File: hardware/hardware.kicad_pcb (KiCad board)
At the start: 2 copper layers, 91.4 x 91.4 mm, 80 parts, among them J1 DB25_Female, J2 USB_B_Micro, J3 RJ45_Bel_SI-60062-F-68net, J4 Conn_02x06_Odd_Even, U1 LD1117S33TR_SOT223, U11 ENC28J60x-SO, U12 74HC14, U2 74LS126, U3 74LS126, U4 LM1117-ADJ, U5 74LS126, U6 74LS126, U7 STM32F072R8Tx, U8 74LS245, Y1 8MHz, Y2 25MHz

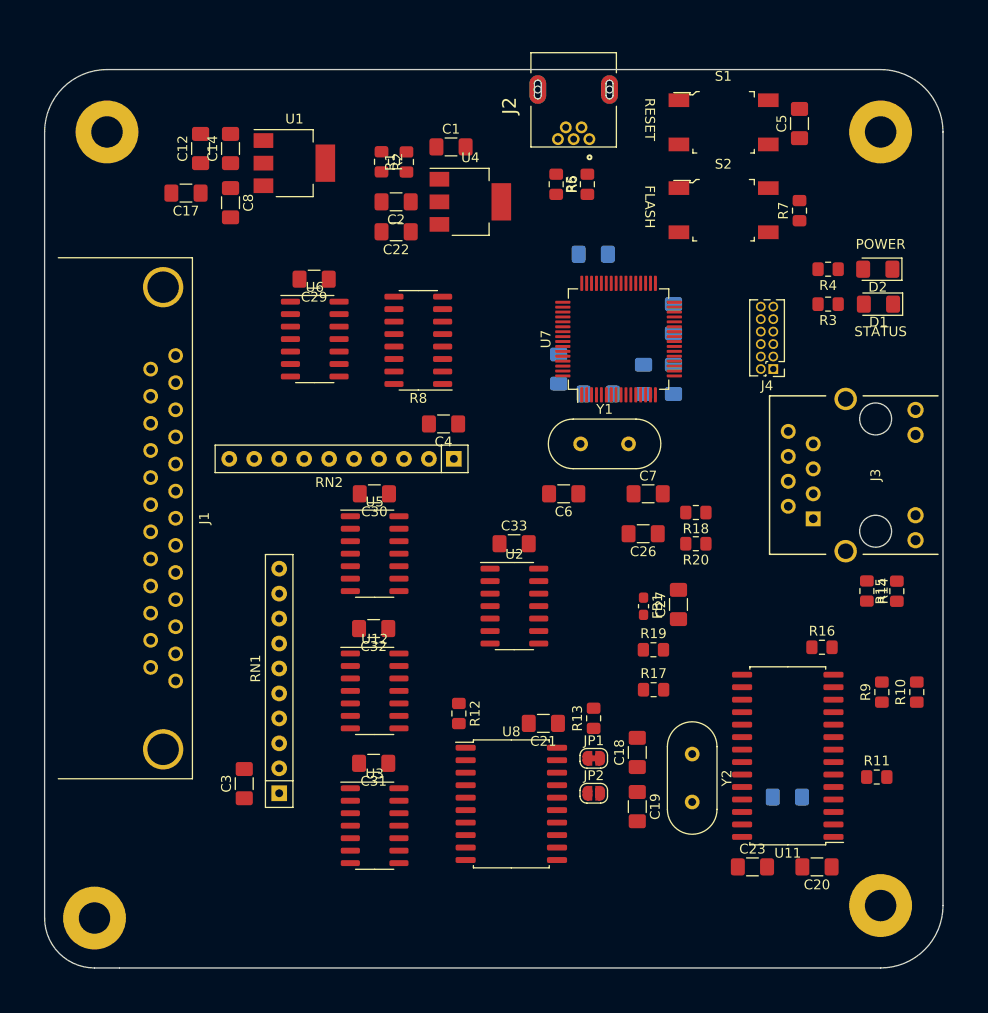
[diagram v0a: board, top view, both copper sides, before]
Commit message: feat: update extension port and place again footprints on pcb
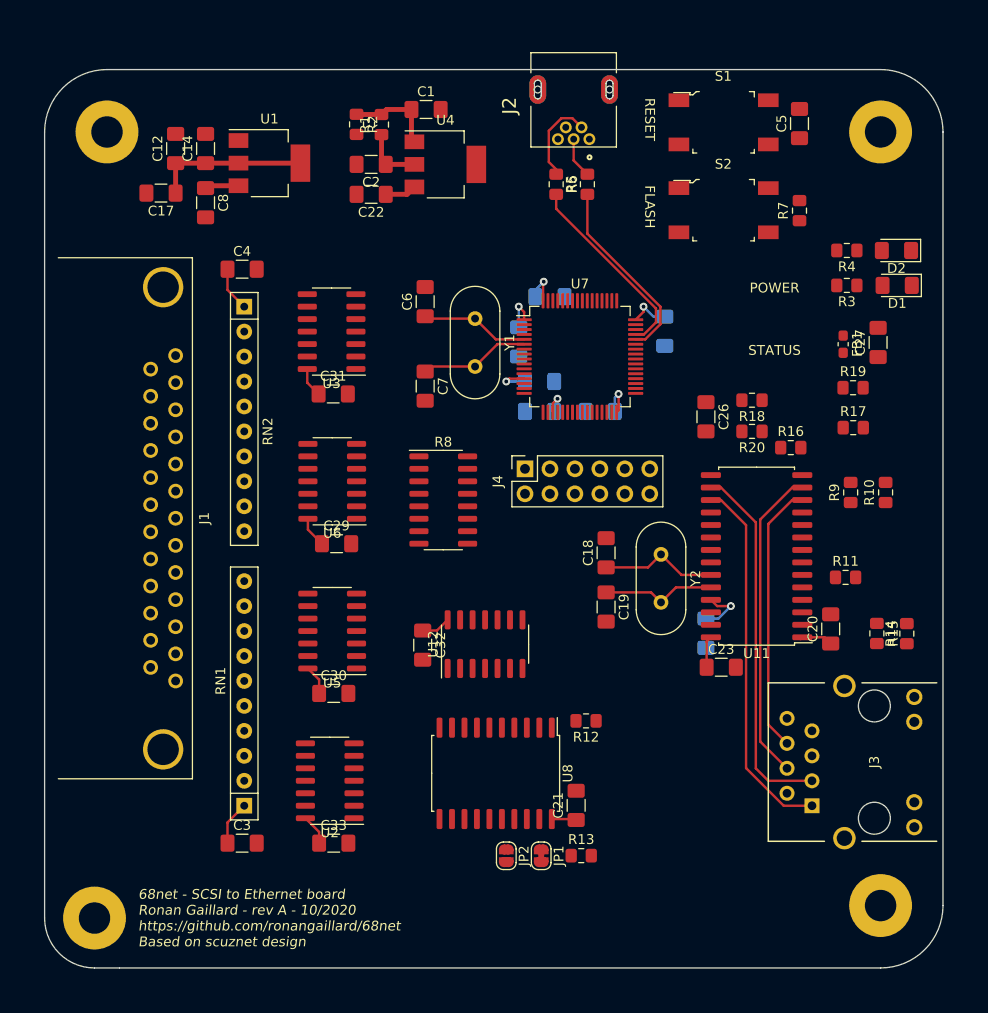
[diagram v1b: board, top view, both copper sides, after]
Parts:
- J4: footprint Connector_PinHeader_1.27mm:PinHeader_2x06_P1.27mm_Vertical -> Connector_PinSocket_2.54mm:PinSocket_2x06_P2.54mm_Vertical
- moved U3 50.5 mm to (49.5, 47.0), turned to 180 degrees
- moved C31 37.8 mm to (49.7, 53.3), turned to 0 degrees
- moved C33 35.6 mm to (49.7, 99.1)
- moved C27 33.5 mm to (105.2, 48.1)
- moved FB1 33.5 mm to (101.6, 48.3)
- moved R19 33.5 mm to (102.6, 52.7)
- moved R17 33.5 mm to (102.6, 56.8)
- moved J3 29.2 mm to (104.8, 96.5)
- moved J4 27.2 mm to (69.2, 61.0), turned to 90 degrees
- moved C29 27.0 mm to (50.0, 68.6), turned to 0 degrees
- moved RN2 26.4 mm to (40.6, 44.5), turned to 270 degrees
- moved U2 25.9 mm to (49.3, 92.7), turned to 180 degrees
- moved C4 25.9 mm to (40.4, 40.6), turned to 0 degrees
- moved C7 25.2 mm to (59.1, 52.5), turned to 270 degrees
- moved C20 24.3 mm to (100.3, 77.3), turned to 90 degrees
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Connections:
- net /DCLK renamed Net-(U7-Pad62)
- net /~DOE~ renamed Net-(U7-Pad29)
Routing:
- net +3V3: track 0.00 -> 64.6 mm, vias 0 -> 7
- net /TPOUT+: track 0.00 -> 37.7 mm
- net /TPOUT-: track 0.00 -> 37.3 mm
- net /TPIN+: track 0.00 -> 32.1 mm
- net /TPIN-: track 0.00 -> 27.6 mm
- net /USB+: track 0.00 -> 19.8 mm
- net /USB-: track 0.00 -> 19.5 mm
- net VBUS: track 0.00 -> 15.2 mm
- net Net-(C18-Pad1): track 0.00 -> 12.1 mm
- net Net-(C19-Pad1): track 0.00 -> 11.7 mm
- net Net-(C7-Pad1): track 0.00 -> 11.2 mm
- net Net-(C6-Pad1): track 0.00 -> 11.0 mm
- net Net-(C1-Pad1): track 0.00 -> 9.22 mm
- net Net-(J2-Pad2): track 0.00 -> 8.97 mm
- net +5V: track 0.00 -> 6.68 mm
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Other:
- board text added: "68net - SCSI to Ethernet board Ronan Gaillard - rev A - 10/2020 https://github.com/ronangaillard/68net Based on scuznet design"

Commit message: feat: finalize revA-alpha
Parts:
- removed J4: Conn_02x06_Odd_Even, Connector_PinSocket_2.54mm:PinSocket_2x06_P2.54mm_Vertical
- removed JP1: SJ, Jumper:SolderJumper-2_P1.3mm_Bridged_RoundedPad1.0x1.5mm
- removed JP2: SJ, Jumper:SolderJumper-2_P1.3mm_Open_RoundedPad1.0x1.5mm
- removed R11: 22, Resistor_SMD:R_0805_2012Metric_Pad1.15x1.40mm_HandSolder
- removed REF00, REF01, REF02, REF03: MountingHole_3.2mm_M3_Pad, MountingHole:MountingHole_3.2mm_M3_Pad
- added C25: 100uF, Capacitor_SMD:CP_Elec_6.3x5.4, F.Cu at (34.3, 28.4)
- added C28: 100nF, Capacitor_SMD:C_1206_3216Metric_Pad1.42x1.75mm_HandSolder, F.Cu at (67.3, 97.5)
- added C34: 100nF, Capacitor_SMD:C_1206_3216Metric_Pad1.42x1.75mm_HandSolder, B.Cu at (79.2, 98.8)
- added C35: 100nF, Capacitor_SMD:C_1206_3216Metric_Pad1.42x1.75mm_HandSolder, B.Cu at (72.9, 98.8)
- added D3: D_Schottky, Diode_SMD:D_SOD-523, F.Cu at (71.7, 35.6)
- added D4: D_Schottky, Diode_SMD:D_SOD-523, F.Cu at (39.9, 35.6)
- added G***: LOGO, hardware:Untitled, F.Cu at (84.8, 45.5)
- added H1: MountingHole, MountingHole:MountingHole_3.2mm_M3_Pad, F.Cu at (105.4, 26.7)
- added H2: MountingHole, MountingHole:MountingHole_3.2mm_M3_Pad, F.Cu at (105.4, 105.4)
- added H3: MountingHole, MountingHole:MountingHole_3.2mm_M3_Pad, F.Cu at (26.7, 26.7)
- added H4: MountingHole, MountingHole:MountingHole_3.2mm_M3_Pad, F.Cu at (26.7, 105.4)
- added R21: 3k3, Resistor_SMD:R_0805_2012Metric_Pad1.15x1.40mm_HandSolder, F.Cu at (46.0, 62.2)
- added R22: 3k3, Resistor_SMD:R_0805_2012Metric_Pad1.15x1.40mm_HandSolder, F.Cu at (46.0, 53.3)
- added R23: 3k3, Resistor_SMD:R_0805_2012Metric_Pad1.15x1.40mm_HandSolder, F.Cu at (46.0, 55.9)
- added R24: 3k3, Resistor_SMD:R_0805_2012Metric_Pad1.15x1.40mm_HandSolder, F.Cu at (46.0, 48.9)
- added R25: 3k3, Resistor_SMD:R_0805_2012Metric_Pad1.15x1.40mm_HandSolder, F.Cu at (46.0, 46.4)
- added R26: 3k3, Resistor_SMD:R_0805_2012Metric_Pad1.15x1.40mm_HandSolder, F.Cu at (46.0, 43.2)
- added R27: 3k3, Resistor_SMD:R_0805_2012Metric_Pad1.15x1.40mm_HandSolder, F.Cu at (46.0, 40.6)
- added R28: 3k3, Resistor_SMD:R_0805_2012Metric_Pad1.15x1.40mm_HandSolder, F.Cu at (68.1, 59.7)
- added R29: 3k3, Resistor_SMD:R_0805_2012Metric_Pad1.15x1.40mm_HandSolder, F.Cu at (58.2, 68.6)
- added R30: 3k3, Resistor_SMD:R_0805_2012Metric_Pad1.15x1.40mm_HandSolder, F.Cu at (58.2, 73.7)
- added R31: 3k3, Resistor_SMD:R_0805_2012Metric_Pad1.15x1.40mm_HandSolder, F.Cu at (46.0, 85.1)
- added R32: 3k3, Resistor_SMD:R_0805_2012Metric_Pad1.15x1.40mm_HandSolder, F.Cu at (46.0, 87.6)
- added R33: 3k3, Resistor_SMD:R_0805_2012Metric_Pad1.15x1.40mm_HandSolder, F.Cu at (46.0, 94.0)
- added R34: 3k3, Resistor_SMD:R_0805_2012Metric_Pad1.15x1.40mm_HandSolder, F.Cu at (46.0, 96.5)
- R4: value 330 -> 165
- R8: value resistor_array_15 -> 3k3; footprint Package_SO:SOIC-16_3.9x9.9mm_P1.27mm -> Resistor_SMD:R_0805_2012Metric_Pad1.15x1.40mm_HandSolder
- U1: value LD1117S33TR_SOT223 -> LD1117 3.3
- U12: value 74HC14 -> 74LVC14
- U2, U3, U5, U6: value 74LS126 -> 74LVTH126
- U8: value 74LS245 -> 74LVC245
- moved FB1 68.9 mm to (62.4, 104.9), turned to 0 degrees
- moved C27 68.8 mm to (62.2, 101.9), turned to 180 degrees
- moved J2 62.6 mm to (110.0, 73.7), turned to 0 degrees
- moved R19 62.1 mm to (67.1, 103.6), turned to 90 degrees
- moved R17 57.2 mm to (69.8, 103.6), turned to 90 degrees
- moved C6 54.2 mm to (108.8, 65.3), turned to 270 degrees
- moved C7 50.0 mm to (108.8, 56.7), turned to 90 degrees
- moved R13 48.4 mm to (63.2, 53.3), turned to 270 degrees
- moved U3 47.1 mm to (53.3, 94.0), turned to 0 degrees
- moved U8 46.4 mm to (71.9, 45.9), turned to 180 degrees
- moved R6 45.6 mm to (97.8, 69.9), turned to 90 degrees
- moved R5 45.4 mm to (100.6, 69.8), turned to 270 degrees
- moved Y1 43.5 mm to (103.8, 63.6), turned to 90 degrees
- moved R16 42.8 mm to (67.6, 90.6), turned to 90 degrees
- moved C21 41.5 mm to (68.6, 54.1), turned to 0 degrees
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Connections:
- C22 pad 1: +5V -> VCC
- C8 pad 1: +5V -> VCC
- J1 pad 25: Net-(J1-Pad25) -> /TPWR
- R13 pad 1: Net-(JP1-Pad2) -> Net-(R13-Pad1)
- R4 pad 2: +5V -> +3V3
- R8 pad 1: /TDB0 -> GND
- R8 pad 2: /TDB1 -> /TDB0
- U1 pad 3: +5V -> VCC
- U11 pad 6: Net-(R11-Pad1) -> /SPI_MISO
- U2 pad 1: /TBSY -> /TDBP
- U2 pad 10: /TDB0 -> GND
- U2 pad 11: /DB4 -> /SEL
- U2 pad 13: /TDB4 -> /TSEL
- U2 pad 3: /BSY -> /DBP
- U2 pad 4: /TREQ -> /TBSY
- U2 pad 6: /REQ -> /BSY
- U2 pad 8: /DB0 -> Net-(U2-Pad8)
- U3 pad 1: GND -> /TIO
- U3 pad 10: /TDB1 -> /TREQ
- U3 pad 11: /DB5 -> /CD
- U3 pad 13: /TDB5 -> /TCD
- U3 pad 3: Net-(U3-Pad3) -> /IO
- U3 pad 8: /DB1 -> /REQ
- U4 pad 3: +5V -> VCC
- U5 pad 1: /TSEL -> /TDB3
- U5 pad 10: /TDB2 -> /TDB0
- U5 pad 11: /DB6 -> /DB2
- U5 pad 13: /TDB6 -> /TDB2
- U5 pad 3: /SEL -> /DB3
- U5 pad 4: /TCD -> /TDB1
- U5 pad 6: /CD -> /DB1
- U5 pad 8: /DB2 -> /DB0
- U6 pad 1: /TDBP -> /TDB7
- U6 pad 10: /TDB3 -> /TDB4
- U6 pad 11: /DB7 -> /DB6
- U6 pad 13: /TDB7 -> /TDB6
- U6 pad 3: /DBP -> /DB7
- U6 pad 4: /TIO -> /TDB5
- U6 pad 6: /IO -> /DB5
- U6 pad 8: /DB3 -> /DB4
- U7 pad 10: /RDB2 -> Net-(U7-Pad10)
- U7 pad 11: /RDB3 -> Net-(U7-Pad11)
- U7 pad 14: /TDB0 -> /RDB0
- U7 pad 15: /TDB1 -> /RDB1
- U7 pad 16: /TDB2 -> /RDB2
- U7 pad 17: /TDB3 -> /RDB3
- U7 pad 2: Net-(U7-Pad2) -> /STATUS_LED
- U7 pad 20: /TDB4 -> /RDB4
- U7 pad 21: /TDB5 -> /RDB5
- U7 pad 22: /TDB6 -> /RDB6
- U7 pad 23: /TDB7 -> /RDB7
- U7 pad 24: /RDB4 -> Net-(U7-Pad24)
- U7 pad 25: /RDB5 -> Net-(U7-Pad25)
- U7 pad 26: /TREQ -> /TDB0
- U7 pad 27: /RDBP -> /TDB1
- U7 pad 28: /RSEL -> /TDB2
- U7 pad 3: /RACK -> Net-(U7-Pad3)
- U7 pad 30: /~SPI_INT~ -> Net-(U7-Pad30)
- U7 pad 37: /RDB6 -> /TDBP
- U7 pad 38: /RDB7 -> /TSEL
- U7 pad 39: /RDBP -> /TBSY
- U7 pad 4: /STATUS_LED -> Net-(U7-Pad4)
- U7 pad 40: /GPIO_0 -> /RDBP
- U7 pad 41: /TDBP -> /RSEL
- U7 pad 42: /TSEL -> /RBSY
- U7 pad 43: /TBSY -> /RACK
- U7 pad 46: /TCD -> /RATN
- U7 pad 49: /TIO -> /RRST
- U7 pad 50: /TMSG -> /TIO
- U7 pad 51: /GPIO_1 -> /TCD
- U7 pad 52: /GPIO_2 -> /TMSG
- U7 pad 53: /GPIO_3 -> /TREQ
- U7 pad 55: /RBSY -> /TDB3
- U7 pad 56: /RATN -> /TDB4
- U7 pad 57: /RRST -> /TDB5
- U7 pad 58: /UART_TX -> /TDB6
- U7 pad 59: /UART_RX -> /TDB7
- U7 pad 62: Net-(U7-Pad62) -> /~SPI_INT~
- U7 pad 8: /RDB0 -> Net-(U7-Pad8)
- U7 pad 9: /RDB1 -> Net-(U7-Pad9)
- U8 pad 11: /DB0 -> /DB7
- U8 pad 12: /DB1 -> /DB6
- U8 pad 13: /DB2 -> /DB5
- U8 pad 14: /DB3 -> /DB4
- U8 pad 15: /DB4 -> /DB3
- U8 pad 16: /DB5 -> /DB2
- U8 pad 17: /DB6 -> /DB1
- U8 pad 18: /DB7 -> /DB0
- U8 pad 19: Net-(JP1-Pad1) -> Net-(R13-Pad1)
- U8 pad 2: /RDB7 -> /RDB0
- U8 pad 3: /RDB6 -> /RDB1
- U8 pad 4: /RDB5 -> /RDB2
- U8 pad 5: /RDB4 -> /RDB3
- U8 pad 6: /RDB3 -> /RDB4
- U8 pad 7: /RDB2 -> /RDB5
- U8 pad 8: /RDB1 -> /RDB6
- U8 pad 9: /RDB0 -> /RDB7
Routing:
- net +3V3: track 64.6 -> 504.1 mm, vias 7 -> 19
- net GND: track 0.00 -> 104.5 mm, vias 0 -> 393
- net /BOOT0: track 0.00 -> 87.6 mm
- net VBUS: track 15.2 -> 102.4 mm, vias 0 -> 2
- net /TDB6: track 0.00 -> 81.3 mm, vias 0 -> 2
- net /TDB7: track 0.00 -> 80.7 mm, vias 0 -> 2
- net /TDB5: track 0.00 -> 77.6 mm, vias 0 -> 2
- net /TDB4: track 0.00 -> 73.4 mm, vias 0 -> 2
- net /TCD: track 0.00 -> 66.8 mm, vias 0 -> 2
- net /TREQ: track 0.00 -> 63.8 mm, vias 0 -> 2
- net +5V: track 6.68 -> 69.2 mm, vias 0 -> 4
- net /TMSG: track 0.00 -> 62.5 mm, vias 0 -> 2
- net /TIO: track 0.00 -> 59.9 mm, vias 0 -> 2
- net /TDB3: track 0.00 -> 59.8 mm, vias 0 -> 2
- net /TDB2: track 0.00 -> 57.7 mm, vias 0 -> 2
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- added copper zone on B.Cu, net GND
- added copper zone on F.Cu, net GND
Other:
- outline, holes or cut-outs redrawn
- board text added: "68net"
- board text added: "Modern SCSI2Ethernet"

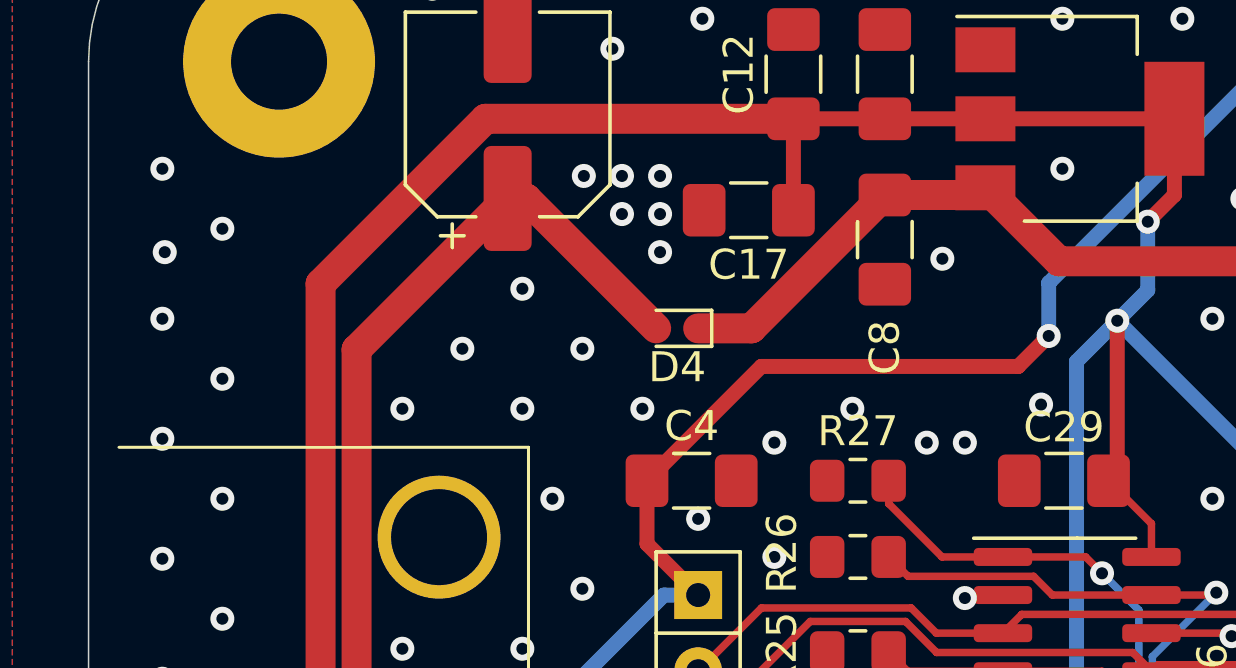
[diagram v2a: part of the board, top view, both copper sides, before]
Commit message: feat: add jumper connector to enable termination
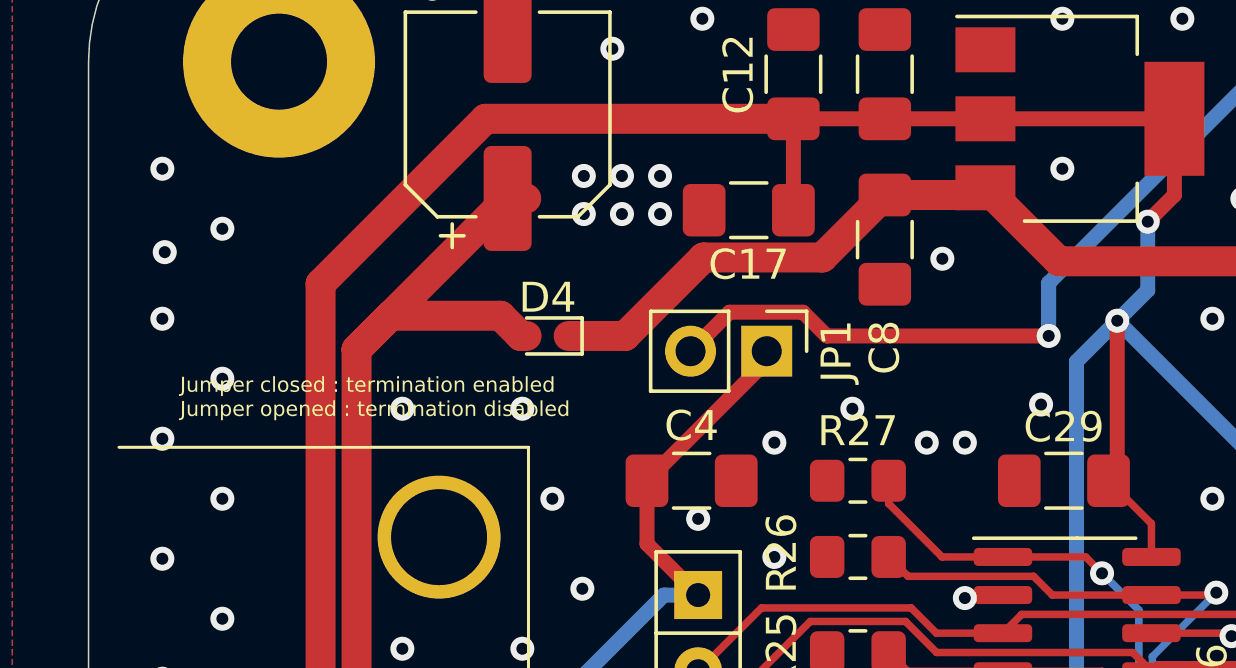
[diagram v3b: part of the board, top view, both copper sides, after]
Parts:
- added JP1: Jumper_2_Bridged, Connector_PinHeader_2.54mm:PinHeader_1x02_P2.54mm_Vertical, F.Cu at (42.9, 36.3)
- moved D4 4.33 mm to (35.6, 35.8)
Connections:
- C3 pad 1: VBUS -> Net-(C3-Pad1)
- C4 pad 1: VBUS -> Net-(C3-Pad1)
- RN1 pad 1: VBUS -> Net-(C3-Pad1)
- RN2 pad 1: VBUS -> Net-(C3-Pad1)
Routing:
- net Net-(C3-Pad1): track 0.00 -> 69.7 mm
- net VBUS: track 102.4 -> 36.1 mm
- net VCC: track 38.0 -> 42.4 mm
- net GND: vias 393 -> 389
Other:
- board text added: "Jumper closed : termination enabled Jumper opened : termination disabled"

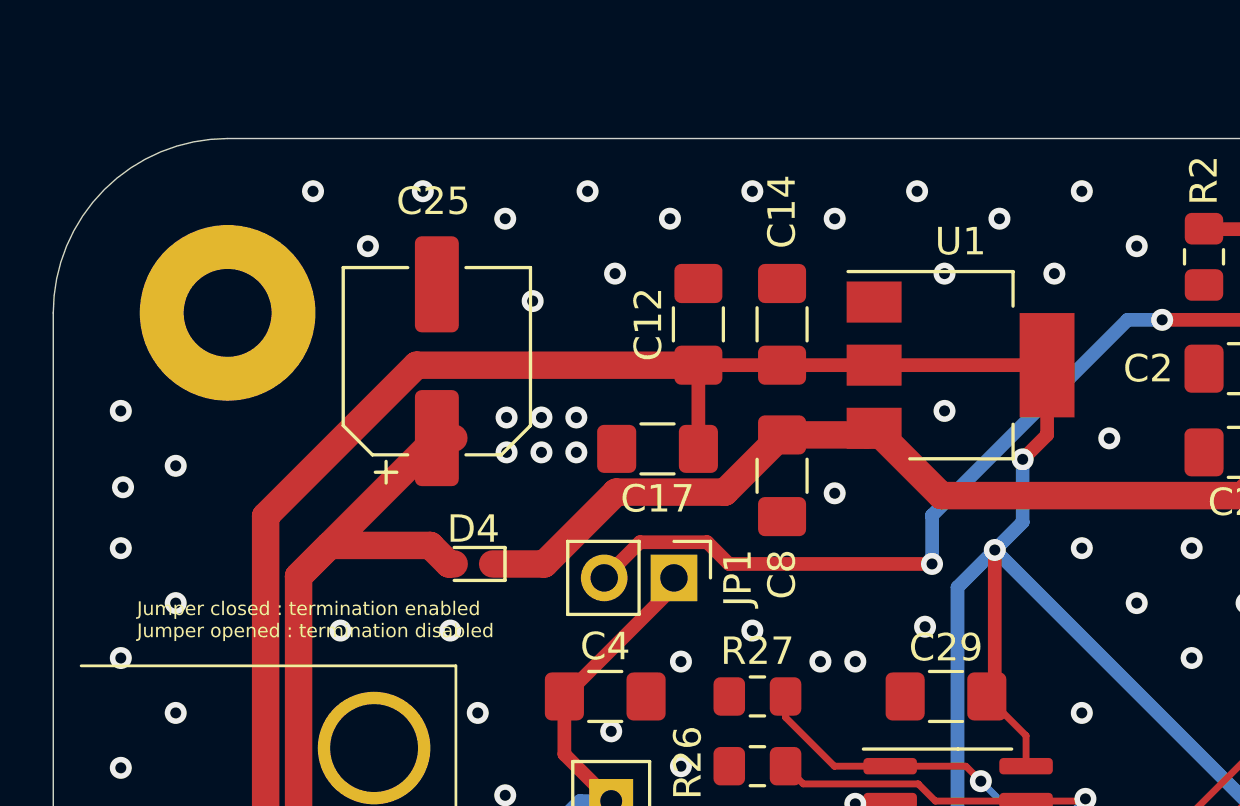
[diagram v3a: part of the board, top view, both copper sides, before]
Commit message: feat: update LDO regulator
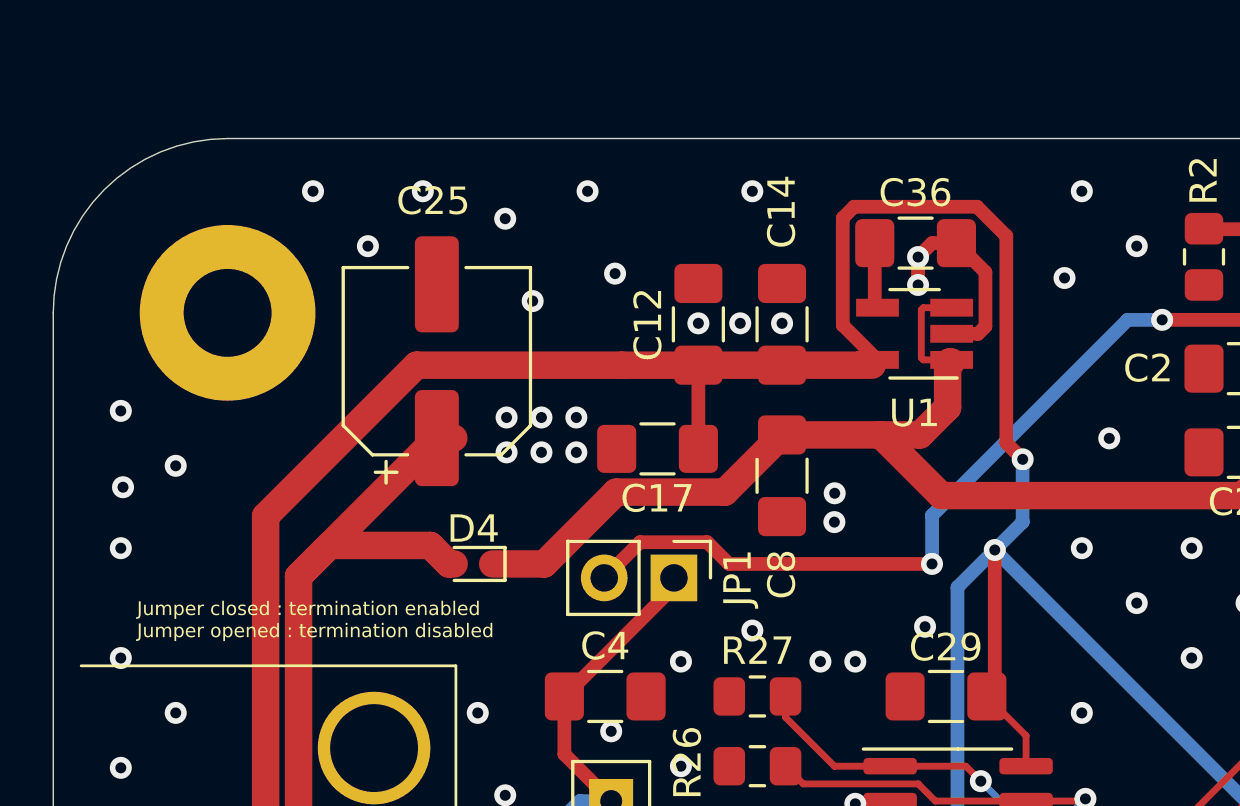
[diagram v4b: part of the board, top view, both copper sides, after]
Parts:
- added C36: 0.1uF, Capacitor_SMD:C_1206_3216Metric_Pad1.42x1.75mm_HandSolder, F.Cu at (51.7, 24.1)
- U1: value LD1117 3.3 -> MIC5319; footprint Package_TO_SOT_SMD:SOT-223-3_TabPin2 -> Package_TO_SOT_SMD:SOT-23-5_HandSoldering
- moved U1 2.03 mm to (51.7, 27.4), turned to 180 degrees
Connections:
- U1 pad 1: GND -> VCC
- U1 pad 2: +3V3 -> GND
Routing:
- net +3V3: track 504.1 -> 514.5 mm
- net GND: track 104.5 -> 112.9 mm, vias 389 -> 386
- net VCC: track 42.4 -> 50.8 mm
- net Net-(C36-Pad1): track 0.00 -> 2.39 mm
